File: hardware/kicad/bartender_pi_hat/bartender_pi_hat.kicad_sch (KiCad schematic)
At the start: 5 parts, among them J1 Raspberry_Pi, J3 Pump Connector, J4 Scale Connector, J5 12V Output, J6 LED Connector

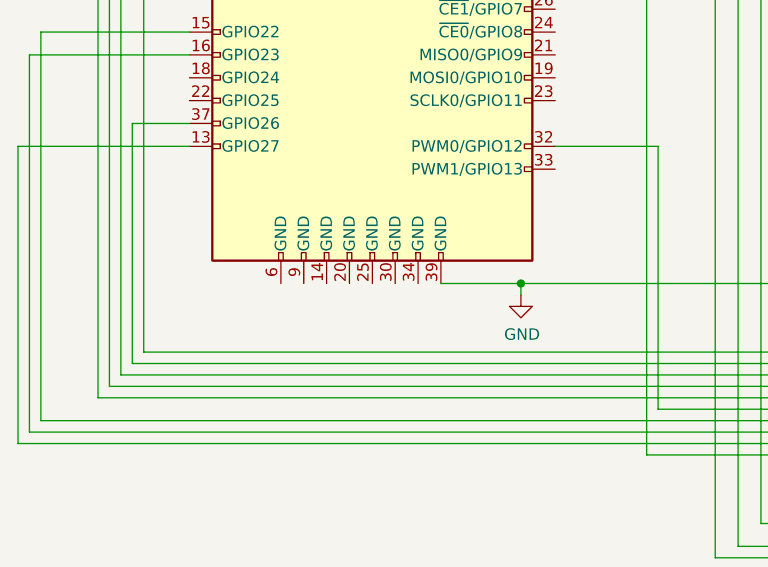
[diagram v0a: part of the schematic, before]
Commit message: Update GND for all RPi Pins
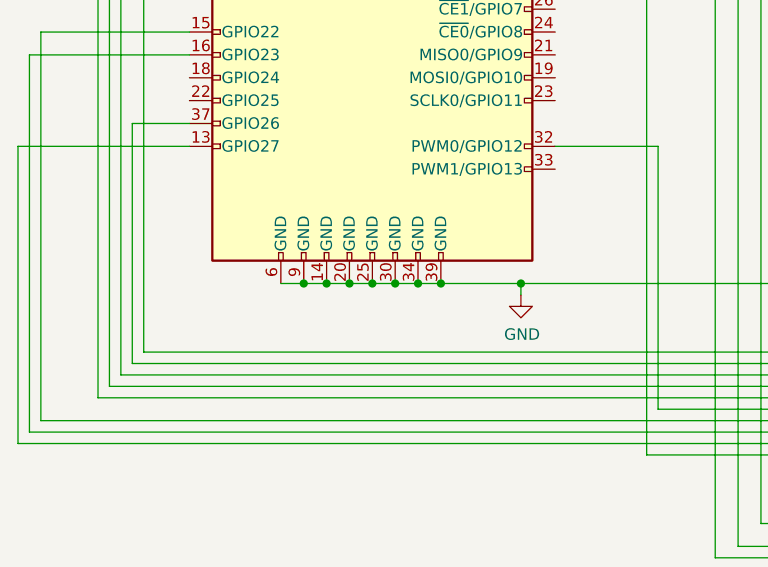
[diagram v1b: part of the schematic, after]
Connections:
- net GND: now also J1.14 (GND), J1.20 (GND), J1.25 (GND), J1.30 (GND), J1.34 (GND), J1.6 (GND), J1.9 (GND)
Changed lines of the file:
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@@
 (kicad_sch (version 20211123) (generator eeschema)
   (paper "A4")
+  (junction (at 68.58 125.73) (diameter 0) (color 0 0 0 0)
+  )
+  (junction (at 76.2 125.73) (diameter 0) (color 0 0 0 0)
+  )
   (junction (at 165.1 111.76) (diameter 0) (color 0 0 0 0)
   )
+  (junction (at 73.66 125.73) (diameter 0) (color 0 0 0 0)
+  )
+  (junction (at 66.04 125.73) (diameter 0) (color 0 0 0 0)
+  )
   (junction (at 85.09 125.73) (diameter 0) (color 0 0 0 0)
   )
+  (junction (at 60.96 125.73) (diameter 0) (color 0 0 0 0)
+  )
   (junction (at 66.04 54.61) (diameter 0) (color 0 0 0 0)
   )
   (junction (at 121.92 125.73) (diameter 0) (color 0 0 0 0)
   )
+  (junction (at 71.12 125.73) (diameter 0) (color 0 0 0 0)
+  )
+  (junction (at 63.5 125.73) (diameter 0) (color 0 0 0 0)
+  )
   (wire (pts (xy 40.64 90.17) (xy 40.64 135.89))
     (stroke (width 0) (type default) (color 0 0 0 0))
@@
     (stroke (width 0) (type default) (color 0 0 0 0))
   )
+  (wire (pts (xy 66.04 125.73) (xy 68.58 125.73))
+    (stroke (width 0) (type default) (color 0 0 0 0))
+  )
   (wire (pts (xy 165.1 111.76) (xy 165.1 120.65))
     (stroke (width 0) (type default) (color 0 0 0 0))
@@
     (stroke (width 0) (type default) (color 0 0 0 0))
   )
+  (wire (pts (xy 68.58 125.73) (xy 71.12 125.73))
+    (stroke (width 0) (type default) (color 0 0 0 0))
+  )
   (wire (pts (xy 140.97 111.76) (xy 165.1 111.76))
     (stroke (width 0) (type default) (color 0 0 0 0))
@@
     (stroke (width 0) (type default) (color 0 0 0 0))
   )
+  (wire (pts (xy 58.42 125.73) (xy 60.96 125.73))
+    (stroke (width 0) (type default) (color 0 0 0 0))
+  )
   (wire (pts (xy 38.1 77.47) (xy 48.26 77.47))
     (stroke (width 0) (type default) (color 0 0 0 0))
   )
+  (wire (pts (xy 71.12 125.73) (xy 73.66 125.73))
+    (stroke (width 0) (type default) (color 0 0 0 0))
+  )
   (wire (pts (xy 43.18 52.07) (xy 148.59 52.07))
     (stroke (width 0) (type default) (color 0 0 0 0))
@@
     (stroke (width 0) (type default) (color 0 0 0 0))
   )
+  (wire (pts (xy 73.66 125.73) (xy 76.2 125.73))
+    (stroke (width 0) (type default) (color 0 0 0 0))
+  )
   (wire (pts (xy 29.21 110.49) (xy 29.21 143.51))
     (stroke (width 0) (type default) (color 0 0 0 0))
@@
     (stroke (width 0) (type default) (color 0 0 0 0))
   )
+  (wire (pts (xy 60.96 125.73) (xy 63.5 125.73))
+    (stroke (width 0) (type default) (color 0 0 0 0))
+  )
   (wire (pts (xy 31.75 97.79) (xy 31.75 140.97))
     (stroke (width 0) (type default) (color 0 0 0 0))
@@
     (stroke (width 0) (type default) (color 0 0 0 0))
   )
+  (wire (pts (xy 63.5 125.73) (xy 66.04 125.73))
+    (stroke (width 0) (type default) (color 0 0 0 0))
+  )

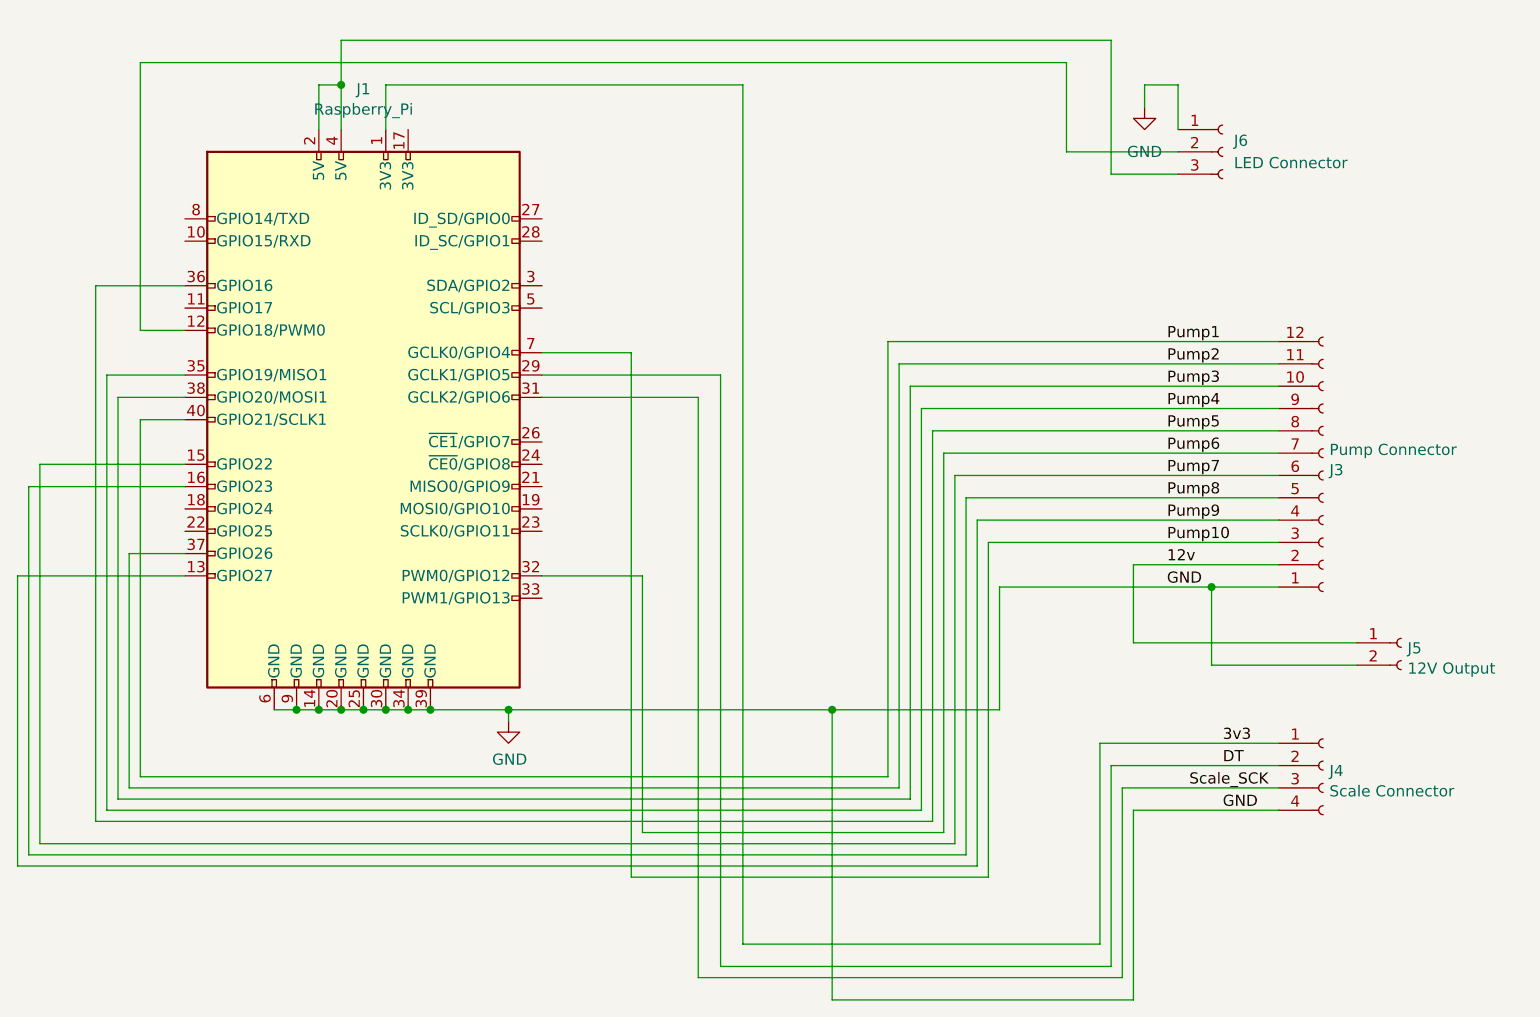
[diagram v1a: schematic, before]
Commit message: Update to pull scale and valve from config, update boards
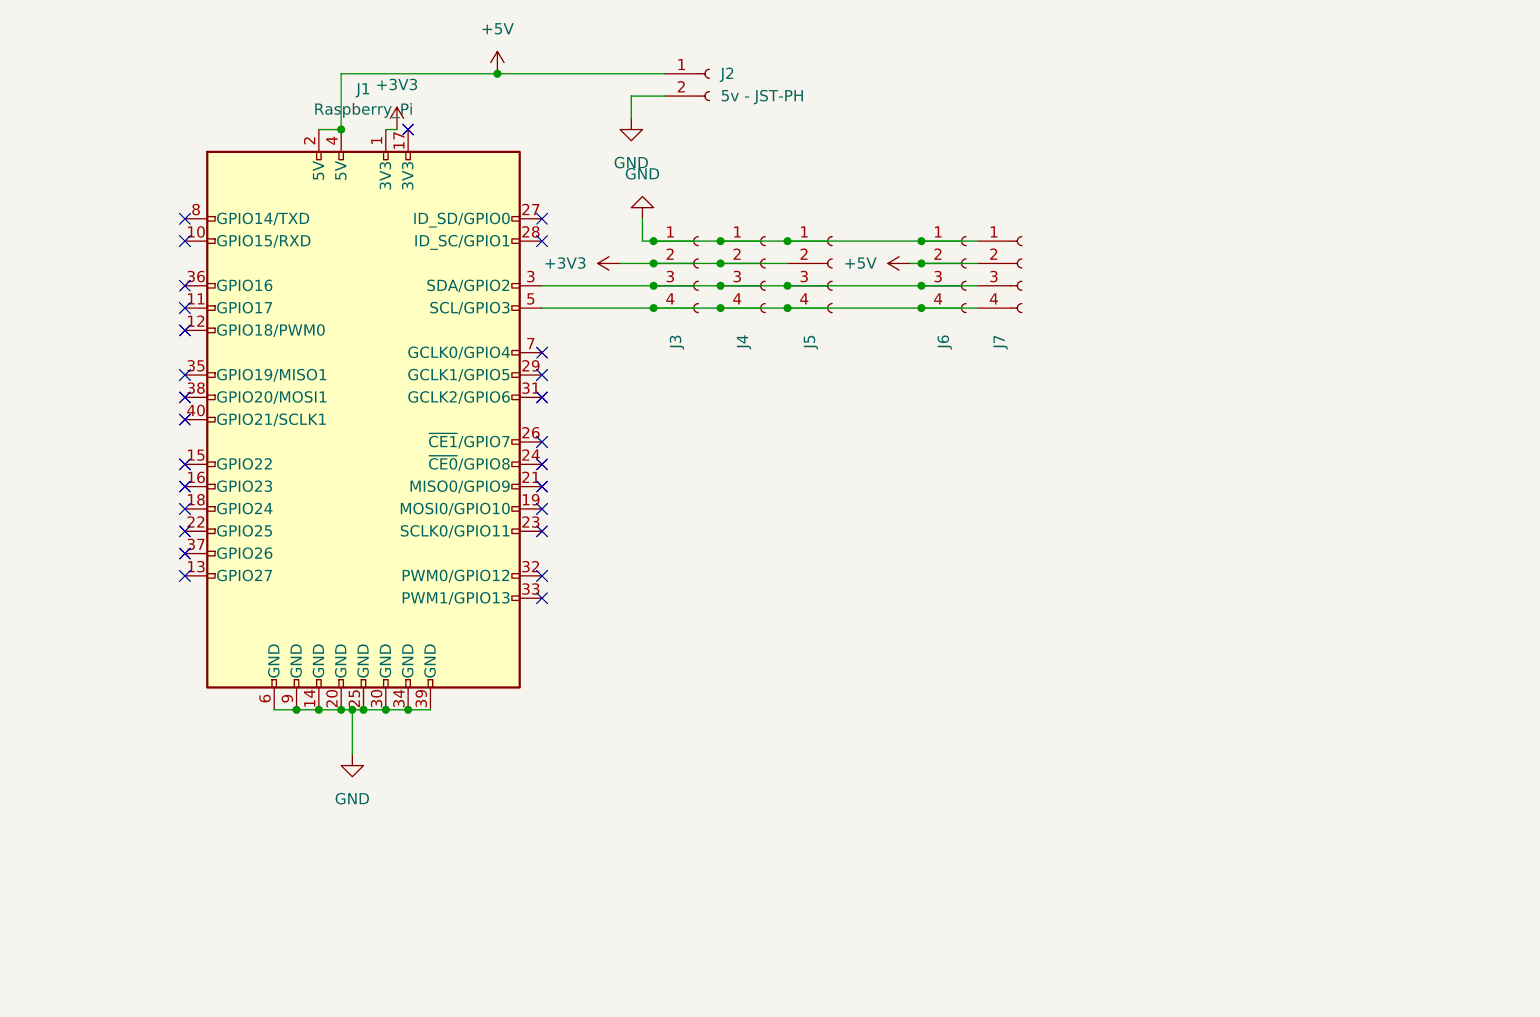
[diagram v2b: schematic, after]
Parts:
- removed J3: Pump Connector, Connector_JST:JST_XH_B12B-XH-A_1x12_P2.50mm_Vertical, symbol Connector:Conn_01x12_Female
- removed J5: 12V Output, Connector_JST:JST_XH_B2B-XH-A_1x02_P2.50mm_Vertical, symbol Connector:Conn_01x02_Female
- removed J6: LED Connector, Connector_JST:JST_XH_B3B-XH-A_1x03_P2.50mm_Vertical, symbol Connector:Conn_01x03_Female
- added J2: 5v - JST-PH, Connector_JST:JST_PH_S2B-PH-K_1x02_P2.00mm_Horizontal, symbol Connector:Conn_01x02_Female
- added J3, J5: Conn_01x04_Female, Connector_JST:JST_SH_SM04B-SRSS-TB_1x04-1MP_P1.00mm_Horizontal, symbol Connector:Conn_01x04_Female
- added J6, J7: Stemma, Connector_JST:JST_PH_S4B-PH-K_1x04_P2.00mm_Horizontal, symbol Connector:Conn_01x04_Female
- J4: value Scale Connector -> Conn_01x04_Female; footprint Connector_JST:JST_XH_B4B-XH-A_1x04_P2.50mm_Vertical -> Connector_JST:JST_SH_SM04B-SRSS-TB_1x04-1MP_P1.00mm_Horizontal
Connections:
- net GND: now also J4.1 (Pin_1), J2.2 (Pin_2), J3.1 (Pin_1), J5.1 (Pin_1), J6.1 (Pin_1), J7.1 (Pin_1); no longer J4.4 (Pin_4)
- net +5V: now reaches J1.2 (5V), J1.4 (5V)
- net +5V: now also J2.1 (Pin_1), J6.2 (Pin_2), J7.2 (Pin_2)
- net at J1.3 (SDA/GPIO2): now also J4.3 (Pin_3), J3.3 (Pin_3), J5.3 (Pin_3), J6.3 (Pin_3), J7.3 (Pin_3)
- net at J1.5 (SCL/GPIO3): now also J4.4 (Pin_4), J3.4 (Pin_4), J5.4 (Pin_4), J6.4 (Pin_4), J7.4 (Pin_4)
- net 3v3 renamed +3V3
- net +3V3: now also J4.2 (Pin_2), J3.2 (Pin_2), J5.2 (Pin_2); no longer J4.1 (Pin_1)
- net DT: no longer names the net of J1.29 (GCLK1/GPIO5)
- net DT: no longer J4.2 (Pin_2)
- net Pump1: no longer names the net of J1.40 (GPIO21/SCLK1)
- net Pump10: no longer names the net of J1.7 (GCLK0/GPIO4)
- net Pump2: no longer names the net of J1.37 (GPIO26)
- net Pump3: no longer names the net of J1.38 (GPIO20/MOSI1)
- net Pump4: no longer names the net of J1.35 (GPIO19/MISO1)
- net Pump5: no longer names the net of J1.36 (GPIO16)
- net Pump6: no longer names the net of J1.32 (PWM0/GPIO12)
- net Pump7: no longer names the net of J1.15 (GPIO22)
- net Pump8: no longer names the net of J1.16 (GPIO23)
- net Pump9: no longer names the net of J1.13 (GPIO27)
- net Scale_SCK: no longer names the net of J1.31 (GCLK2/GPIO6)
- net Scale_SCK: no longer J4.3 (Pin_3)
- no-connect marks 0 -> 27
